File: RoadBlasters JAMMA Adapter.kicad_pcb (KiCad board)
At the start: 2 copper layers, 111 x 82 mm, 47 parts, among them J101GND Molex_KK-254_AE-6410-04A_1x04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, J101V Molex_KK-254_AE-6410-06A_1x06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, J102 Molex_KK-254_AE-6410-02A_1x02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, J103 Molex_KK-254_AE-6410-02A_1x02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, J104 Molex_KK-254_AE-6410-02A_1x02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, J105 Molex_KK-254_AE-6410-04A_1x04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, J106 Molex_KK-254_AE-6410-03A_1x03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, J108 Molex_KK-254_AE-6410-05A_1x05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, P1 10K, U1 74LS86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

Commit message: RoadBlasters, Rev. 1
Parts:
- removed J101GND: Molex_KK-254_AE-6410-04A_1x04_P2.54mm_Vertical, Connector_Molex:Molex_KK-254_AE-6410-04A_1x04_P2.54mm_Vertical
- removed PMH2, PMH3: MountingHole_3.2mm_M3_Pad_Via, MountingHole_3.2mm_M3_Pad_Via
- J101: renamed from J101V; value Molex_KK-254_AE-6410-06A_1x06_P2.54mm_Vertical -> Molex_KK-396_5273-10A_1x10_P3.96mm_Vertical; footprint Connector_Molex:Molex_KK-254_AE-6410-06A_1x06_P2.54mm_Vertical -> Connector_Molex:Molex_KK-396_5273-10A_1x10_P3.96mm_Vertical
- moved -12V 34.4 mm to (145.2, 110.8)
- moved J101 19.4 mm to (192.0, 123.0)
- moved +5V 5.88 mm to (188.4, 75.2)
- moved GND 5.88 mm to (191.3, 75.2)
- moved +12V 5.88 mm to (185.8, 75.2)
- moved C1 4.71 mm to (158.2, 112.6)
- moved TEST 3.00 mm to (93.5, 71.0)
- moved PMH4 2.17 mm to (93.8, 78.8)
- moved PMH1 2.15 mm to (196.2, 78.8)
- moved C4 2.00 mm to (174.6, 109.2)
- moved R4 1.89 mm to (174.6, 112.0)
- moved P1 0.19 mm to (161.9, 103.0)
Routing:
- net +5V: track 406.7 -> 472.7 mm
- net GND: track 797.3 -> 758.6 mm
- net SWE: track 49.0 -> 25.7 mm
- net +12V: track 67.5 -> 86.4 mm
- net -12V: track 139.4 -> 148.6 mm
- net U4_GAIN_P8: track 39.8 -> 36.0 mm
- net AUDIO_PREAMP_OUT: track 61.4 -> 57.7 mm
- net U4_GAIN_P1: track 53.9 -> 52.4 mm
- net TEST_SW: track 81.0 -> 79.8 mm
- net VIDEO_B: track 61.4 -> 60.5 mm
- net VIDEO_G: track 63.4 -> 62.5 mm
- net VIDEO_R: track 61.3 -> 60.4 mm
- net VIDEO_SYNC: track 55.5 -> 54.8 mm
- net AUDIO_MONO: track 12.4 -> 11.7 mm
- net AUDIO_PREAMP: track 23.0 -> 22.5 mm
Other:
- board text added: "Atari® System I JAMMA Interface for RoadBlasters®, Rev. 1"
- board text added: "RST"
- board text removed: "Atari® System 1 JAMMA Interface for RoadBlasters®"
- board text removed: "J101"
- board text removed: "RESET"

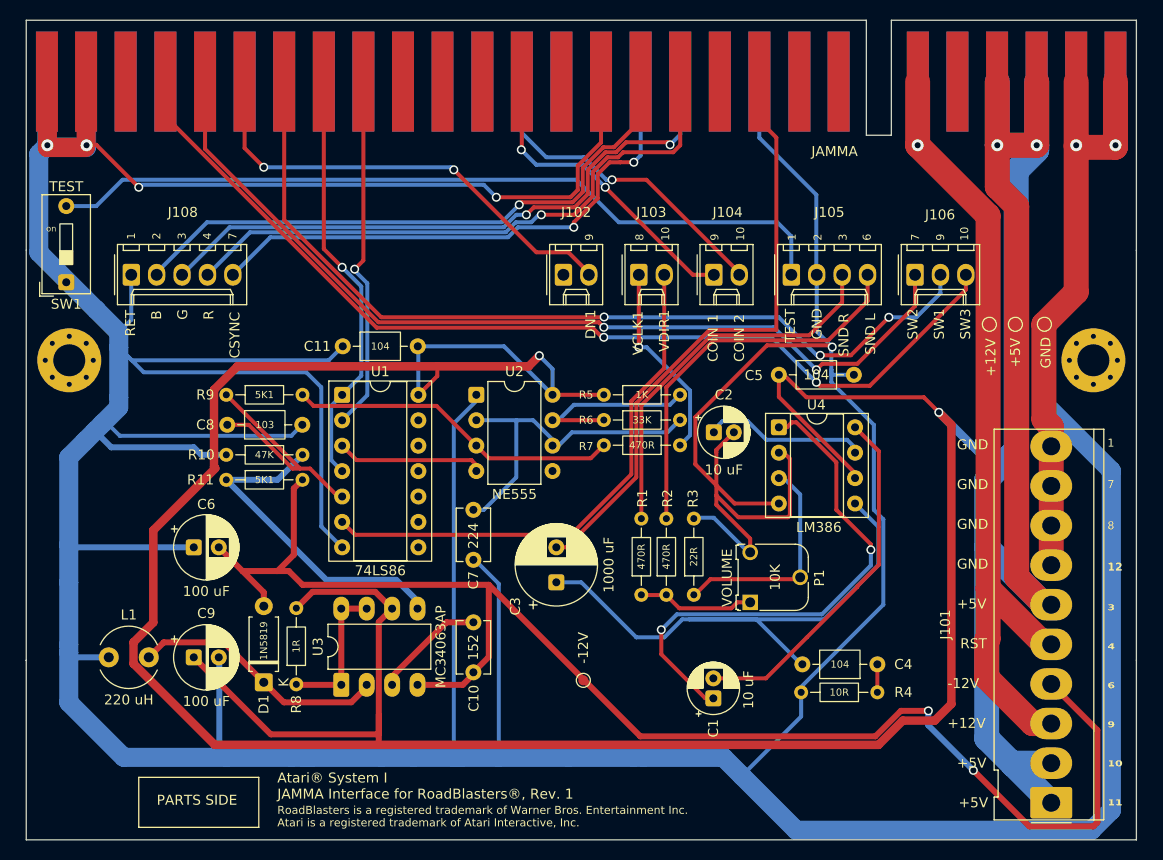
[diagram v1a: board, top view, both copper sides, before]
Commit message: slightly widen boards
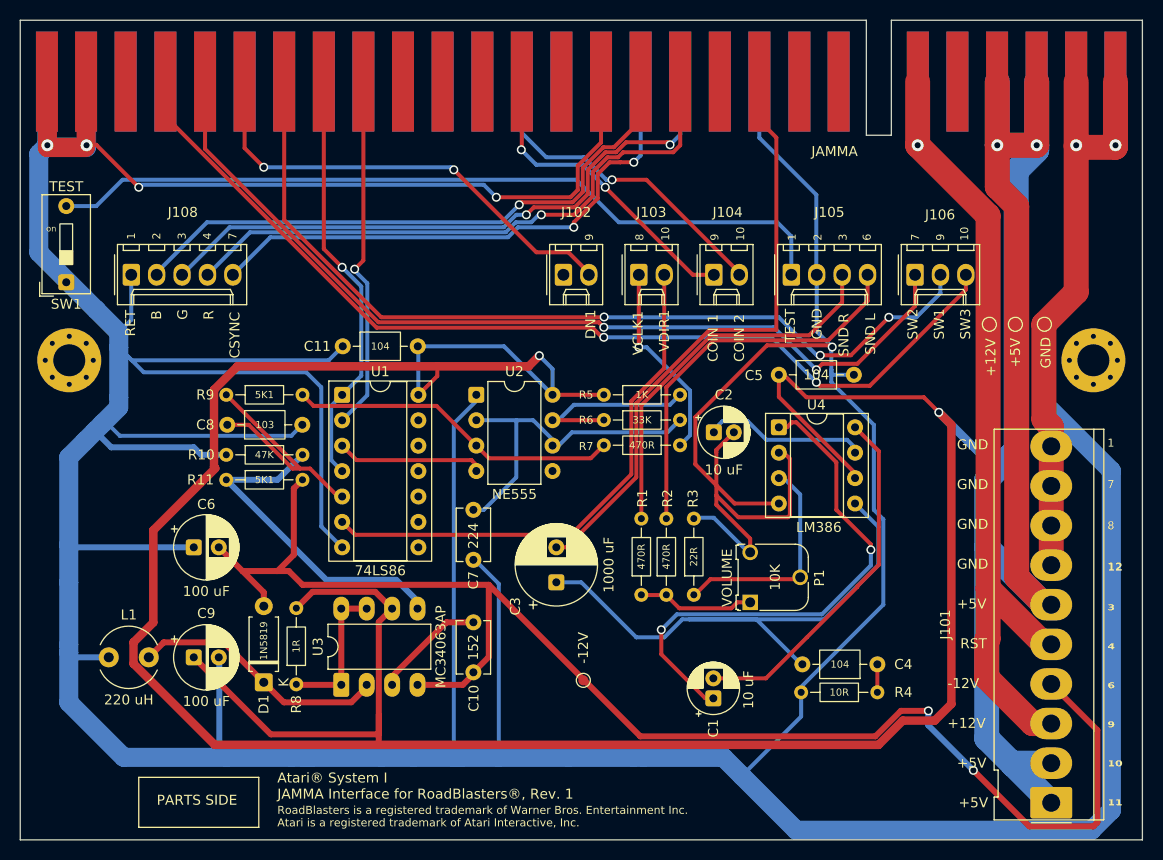
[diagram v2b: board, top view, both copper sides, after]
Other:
- board size 111 x 82 mm -> 112.2 x 82 mm
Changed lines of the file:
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@@
 	(gr_poly
 		(pts
-			(xy 173.5 56.300005) (xy 176 56.300005) (xy 176 44.8) (xy 200.500004 44.8) (xy 200.500004 67.800005)
-			(xy 200.5 67.800005) (xy 200.5 108.800005) (xy 200.5 126.75) (xy 89.5 126.75) (xy 89.5 108.800005)
-			(xy 89.499997 108.800005) (xy 89.499997 67.800005) (xy 89.499997 44.8) (xy 173.5 44.8)
+			(xy 173.5 56.300005) (xy 176 56.300005) (xy 176 44.8) (xy 201.100004 44.8) (xy 201.1 126.75) (xy 88.9 126.75)
+			(xy 88.899997 44.8) (xy 173.5 44.8)
 		)
 		(stroke
